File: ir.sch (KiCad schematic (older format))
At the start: 4 parts, among them Q3 MPT60363T

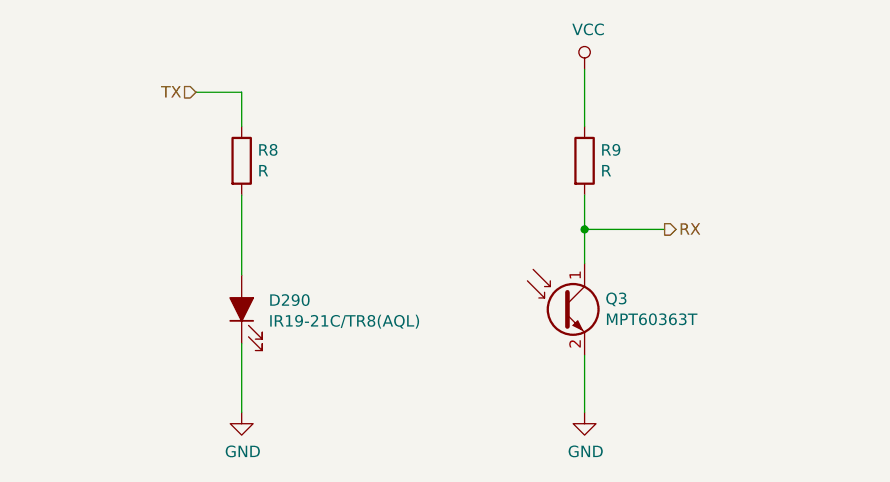
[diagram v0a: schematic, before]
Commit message: Updates to production version
Changed infrared setup, added step-up for battery power, added battery power switch, added more capacitors, changed and added logos, etc.
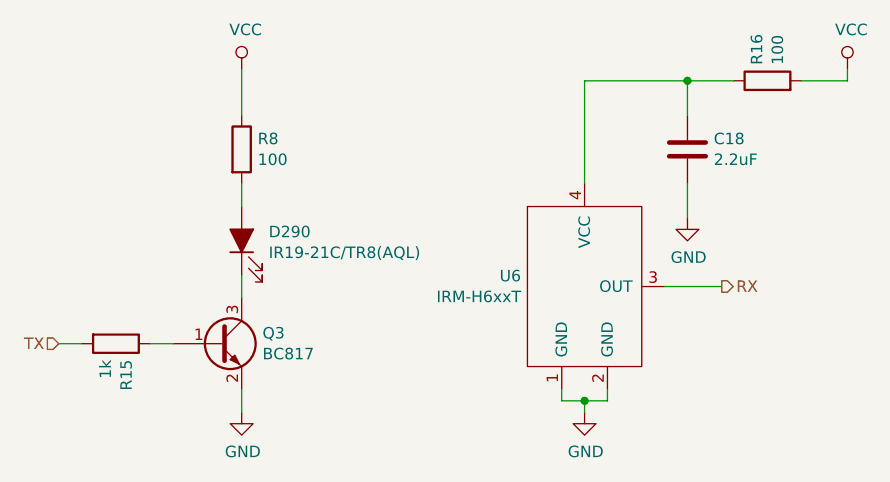
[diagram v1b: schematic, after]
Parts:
- removed Q3: MPT60363T, LEDs:LED_0603, symbol device:Q_Photo_NPN
- removed R9: R, Resistors_SMD:R_0603, symbol device:R
- added C18: 2.2uF, Capacitors_SMD:C_0603, symbol device:C
- added Q3: BC817, TO_SOT_Packages_SMD:SOT-23, symbol Transistor_BJT:BC817
- added R15: 1k, Resistors_SMD:R_0603, symbol device:R
- added R16: 100, Resistors_SMD:R_0603, symbol device:R
- added U6: IRM-H6xxT, Opto:IRM-H6xxT, symbol Opto:IRM-Hxx6T
- R8: value R -> 100
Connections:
- net GND: now also C18.2, Q3.2 (E), U6.1 (GND), U6.2 (GND); no longer D290.1 (K)
- net RX: now also U6.3 (OUT)
- net TX: now also R15.2; no longer R8.1
- net VCC: now also R8.1, R16.2
- new net: D290.1 (K), Q3.3 (C)
- new net: Q3.1 (B), R15.1
- new net: C18.1, R16.1, U6.4 (VCC)
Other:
- moved on the sheet: D290, R8
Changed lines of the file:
@@
 L device:LED_ALT D290
 U 1 1 5EE5B70A
-P 2400 3300
-F 0 "D290" V 2439 3182 50  0000 R CNN
-F 1 "IR19-21C/TR8(AQL)" V 2348 3182 50  0000 R CNN
-F 2 "LEDs:LED_0603" H 2400 3300 50  0001 C CNN
-F 3 "~" H 2400 3300 50  0001 C CNN
-	1    2400 3300
+P 2400 3000
+F 0 "D290" V 2439 2882 50  0000 R CNN
+F 1 "IR19-21C/TR8(AQL)" V 2348 2882 50  0000 R CNN
+F 2 "LEDs:LED_0603" H 2400 3000 50  0001 C CNN
+F 3 "~" H 2400 3000 50  0001 C CNN
+	1    2400 3000
 	0    -1   -1   0
-$EndComp
-$Comp
-L device:Q_Photo_NPN Q3
-U 1 1 5EE5D47A
-P 3800 3300
-F 0 "Q3" H 3991 3346 50  0000 L CNN
-F 1 "MPT60363T" H 3991 3255 50  0000 L CNN
-F 2 "LEDs:LED_0603" H 4000 3400 50  0001 C CNN
-F 3 "~" H 3800 3300 50  0001 C CNN
-	1    3800 3300
-	1    0    0    -1
-$EndComp
-$Comp
-L device:R R9
-U 1 1 5EE5E9AD
-P 3900 2650
-F 0 "R9" H 3970 2696 50  0000 L CNN
-F 1 "R" H 3970 2605 50  0000 L CNN
-F 2 "Resistors_SMD:R_0603" V 3830 2650 50  0001 C CNN
-F 3 "~" H 3900 2650 50  0001 C CNN
-	1    3900 2650
-	1    0    0    -1
 $EndComp
 $Comp
 L device:R R8
 U 1 1 5EE5F24C
-P 2400 2650
-F 0 "R8" H 2470 2696 50  0000 L CNN
-F 1 "R" H 2470 2605 50  0000 L CNN
-F 2 "Resistors_SMD:R_0603" V 2330 2650 50  0001 C CNN
-F 3 "~" H 2400 2650 50  0001 C CNN
-	1    2400 2650
+P 2400 2600
+F 0 "R8" H 2470 2646 50  0000 L CNN
+F 1 "100" H 2470 2555 50  0000 L CNN
+F 2 "Resistors_SMD:R_0603" V 2330 2600 50  0001 C CNN
+F 3 "~" H 2400 2600 50  0001 C CNN
+	1    2400 2600
 	1    0    0    -1
 $EndComp
@@
 $EndComp
 $Comp
-L power:VCC #PWR051
-U 1 1 5EE60502
-P 3900 2250
-F 0 "#PWR051" H 3900 2100 50  0001 C CNN
-F 1 "VCC" H 3917 2423 50  0000 C CNN
-F 2 "" H 3900 2250 50  0001 C CNN
-F 3 "" H 3900 2250 50  0001 C CNN
-	1    3900 2250
-	1    0    0    -1
-$EndComp
-Wire Wire Line
-	2400 3750 2400 3450
-Wire Wire Line
-	2400 3150 2400 2800
-Wire Wire Line
-	2400 2500 2400 2350
-Wire Wire Line
-	2400 2350 2200 2350
-$Comp
 L power:GND #PWR052
 U 1 1 5EE60FD0
@@
 	1    0    0    -1
 $EndComp
+Text HLabel 1600 3450 0    50   Input ~ 0
+TX
+Text HLabel 4500 3200 2    50   Output ~ 0
+RX
+$Comp
+L Transistor_BJT:BC817 Q3
+U 1 1 5F038B96
+P 2300 3450
+F 0 "Q3" H 2491 3496 50  0000 L CNN
+F 1 "BC817" H 2491 3405 50  0000 L CNN
+F 2 "TO_SOT_Packages_SMD:SOT-23" H 2500 3375 50  0001 L CIN
+F 3 "http://www.fairchildsemi.com/ds/BC/BC817.pdf" H 2300 3450 50  0001 L CNN
+	1    2300 3450
+	1    0    0    -1
+$EndComp
+$Comp
+L power:VCC #PWR072
+U 1 1 5F03FA4A
+P 2400 2250
+F 0 "#PWR072" H 2400 2100 50  0001 C CNN
+F 1 "VCC" H 2417 2423 50  0000 C CNN
+F 2 "" H 2400 2250 50  0001 C CNN
+F 3 "" H 2400 2250 50  0001 C CNN
+	1    2400 2250
+	1    0    0    -1
+$EndComp
 Wire Wire Line
-	3900 3750 3900 3500
+	2400 2250 2400 2450
 Wire Wire Line
-	3900 3100 3900 2950
+	2400 2750 2400 2850
 Wire Wire Line
-	3900 2500 3900 2250
+	2400 3150 2400 3250
 Wire Wire Line
-	3900 2950 4250 2950
-Connection ~ 3900 2950
+	2400 3650 2400 3750
+$Comp
+L device:R R15
+U 1 1 5F0409F1
+P 1850 3450
+F 0 "R15" H 1920 3496 50  0000 L CNN
+F 1 "1k" H 1920 3405 50  0000 L CNN
+F 2 "Resistors_SMD:R_0603" V 1780 3450 50  0001 C CNN
+F 3 "~" H 1850 3450 50  0001 C CNN
+	1    1850 3450
+	0    1    1    0
+$EndComp
 Wire Wire Line
-	3900 2950 3900 2800
-Text HLabel 2200 2350 0    50   Input ~ 0
-TX
-Text HLabel 4250 2950 2    50   Output ~ 0
-RX
+	2000 3450 2100 3450
+Wire Wire Line
+	1600 3450 1700 3450
+$Comp
+L Opto:IRM-Hxx6T U6
+U 1 1 5F042EAF
+P 3900 3200
+F 0 "U6" H 3622 3246 50  0000 R CNN
+F 1 "IRM-H6xxT" H 3622 3155 50  0000 R CNN
+F 2 "Opto:IRM-H6xxT" H 3900 3200 50  0001 C CNN
+F 3 "" H 3900 3200 50  0001 C CNN
+	1    3900 3200
+	1    0    0    -1
+$EndComp
+Wire Wire Line
+	4000 3650 4000 3700
+Wire Wire Line
+	4000 3700 3900 3700
+Wire Wire Line
+	3800 3700 3800 3650
+Wire Wire Line
+	3900 3750 3900 3700
+Connection ~ 3900 3700
+Wire Wire Line
+	3900 3700 3800 3700
+Wire Wire Line
+	4250 3200 4500 3200
+$Comp
+L device:C C18
+U 1 1 5F0FDF0F
+P 4350 2600
+F 0 "C18" H 4465 2646 50  0000 L CNN
+F 1 "2.2uF" H 4465 2555 50  0000 L CNN
+F 2 "Capacitors_SMD:C_0603" H 4388 2450 50  0001 C CNN
+F 3 "~" H 4350 2600 50  0001 C CNN
+	1    4350 2600
+	1    0    0    -1
+$EndComp
+$Comp
+L power:VCC #PWR074
+U 1 1 5F0FF8F2
+P 5050 2250
+F 0 "#PWR074" H 5050 2100 50  0001 C CNN
+F 1 "VCC" H 5067 2423 50  0000 C CNN
+F 2 "" H 5050 2250 50  0001 C CNN
+F 3 "" H 5050 2250 50  0001 C CNN
+	1    5050 2250
+	1    0    0    -1
+$EndComp
+$Comp
+L power:GND #PWR073
+U 1 1 5F0FFC16
+P 4350 2900
+F 0 "#PWR073" H 4350 2650 50  0001 C CNN
+F 1 "GND" H 4355 2727 50  0000 C CNN
+F 2 "" H 4350 2900 50  0001 C CNN
+F 3 "" H 4350 2900 50  0001 C CNN
+	1    4350 2900
+	1    0    0    -1
+$EndComp
+Wire Wire Line
+	4350 2300 4350 2450
+Wire Wire Line
+	4350 2750 4350 2900
+$Comp
+L device:R R16
+U 1 1 5F1012CF
+P 4700 2300
+F 0 "R16" H 4770 2346 50  0000 L CNN
+F 1 "100" H 4770 2255 50  0000 L CNN
+F 2 "Resistors_SMD:R_0603" V 4630 2300 50  0001 C CNN
+F 3 "~" H 4700 2300 50  0001 C CNN
+	1    4700 2300
+	0    -1   -1   0
+$EndComp
+Wire Wire Line
+	5050 2250 5050 2300
+Wire Wire Line
+	5050 2300 4850 2300
+Wire Wire Line
+	3900 2300 3900 2750
+Connection ~ 4350 2300
+Wire Wire Line
+	4350 2300 3900 2300
+Wire Wire Line
+	4350 2300 4550 2300
 $EndSCHEMATC
